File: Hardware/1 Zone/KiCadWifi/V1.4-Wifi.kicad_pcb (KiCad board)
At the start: 2 copper layers, 100 x 80 mm, 133 parts, among them CN11 Pinheader 1x12 P2.54 Horizont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, CN16 Pinheader 1x02 P2.54 Horizont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, J1 Screw_Terminal_01x02, Q1 IPD90N04S403ATMA1, Q10 PJA3404A, Q11 PJA3404A, Q12 BC816-16VL, Q8 UMH3NTN, SW1 K2-1102DP-G3SW-04, SW2 K2-1102DP-G3SW-04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

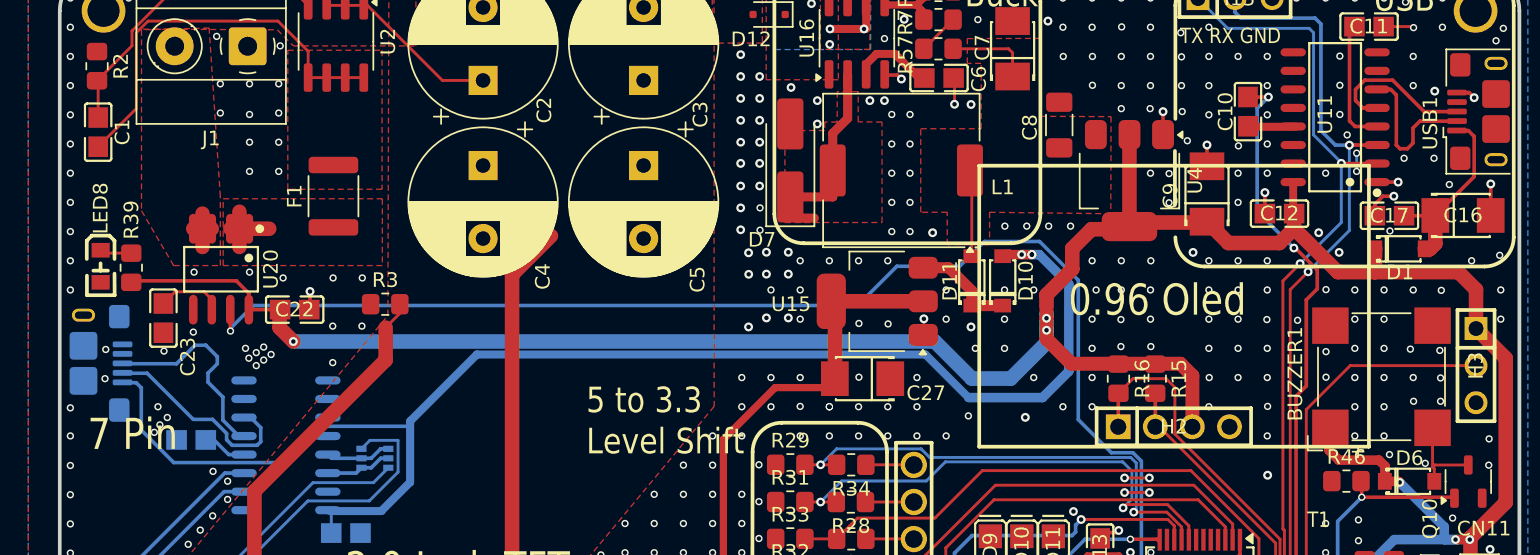
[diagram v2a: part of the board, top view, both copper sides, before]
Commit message: Rerouted D+,D-,E_D+,E_D- differential pairs to reduce gap between them. Renamed D+_E, D-_E for KiCad reasons.
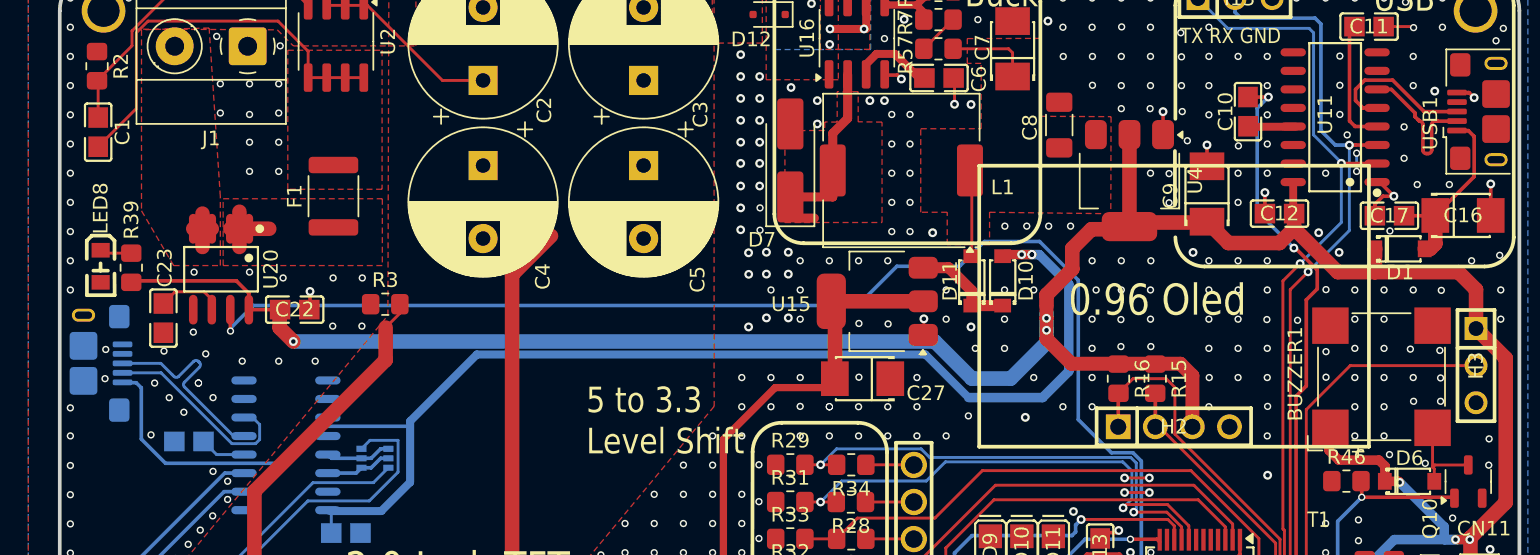
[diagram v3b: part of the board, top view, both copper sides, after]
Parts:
- moved C31 0.18 mm to (108.8, 102.5)
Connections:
- net D+_E renamed E_D+
- net D-_E renamed E_D-
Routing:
- net Net-(U22-V3): track 2.46 -> 3.14 mm
- net GND: track 59.8 -> 59.9 mm, vias 697 -> 696
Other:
- board text removed: "7 Pin"

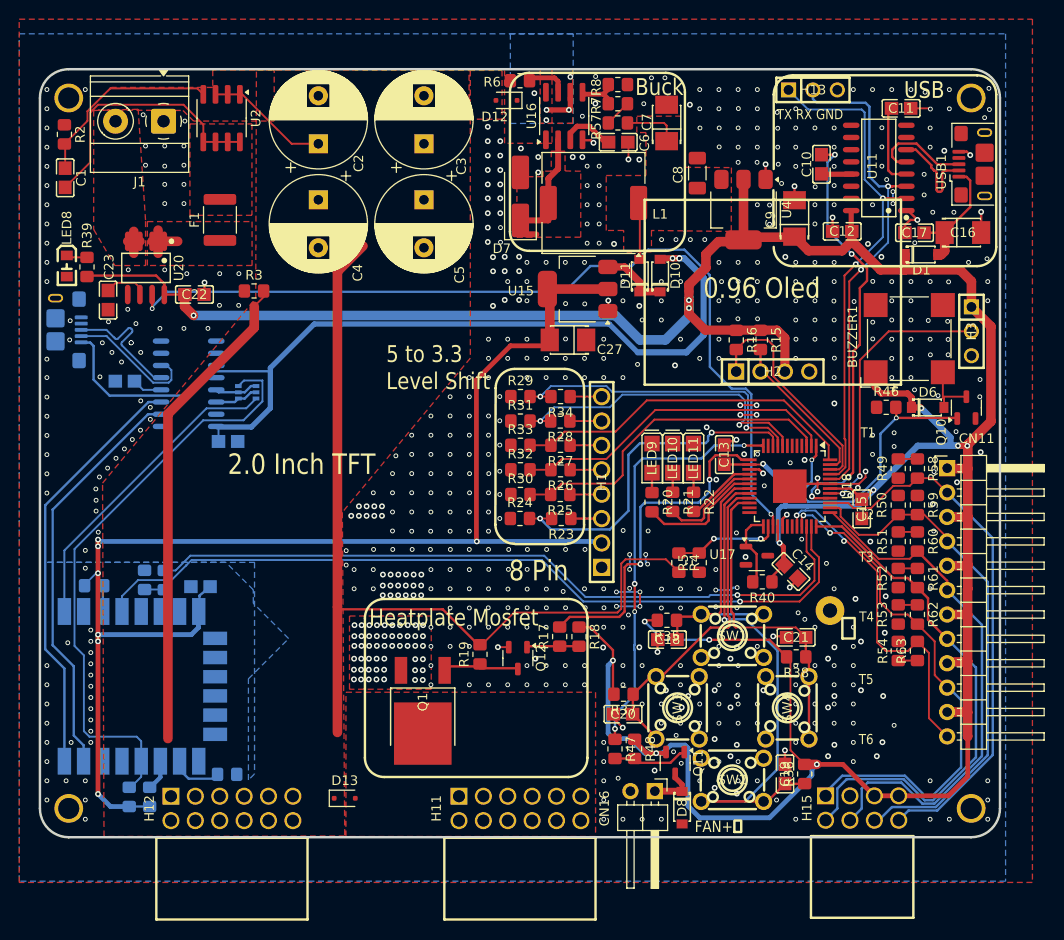
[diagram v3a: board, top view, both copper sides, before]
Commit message: Refactor. Visual improvements to PCB layout.
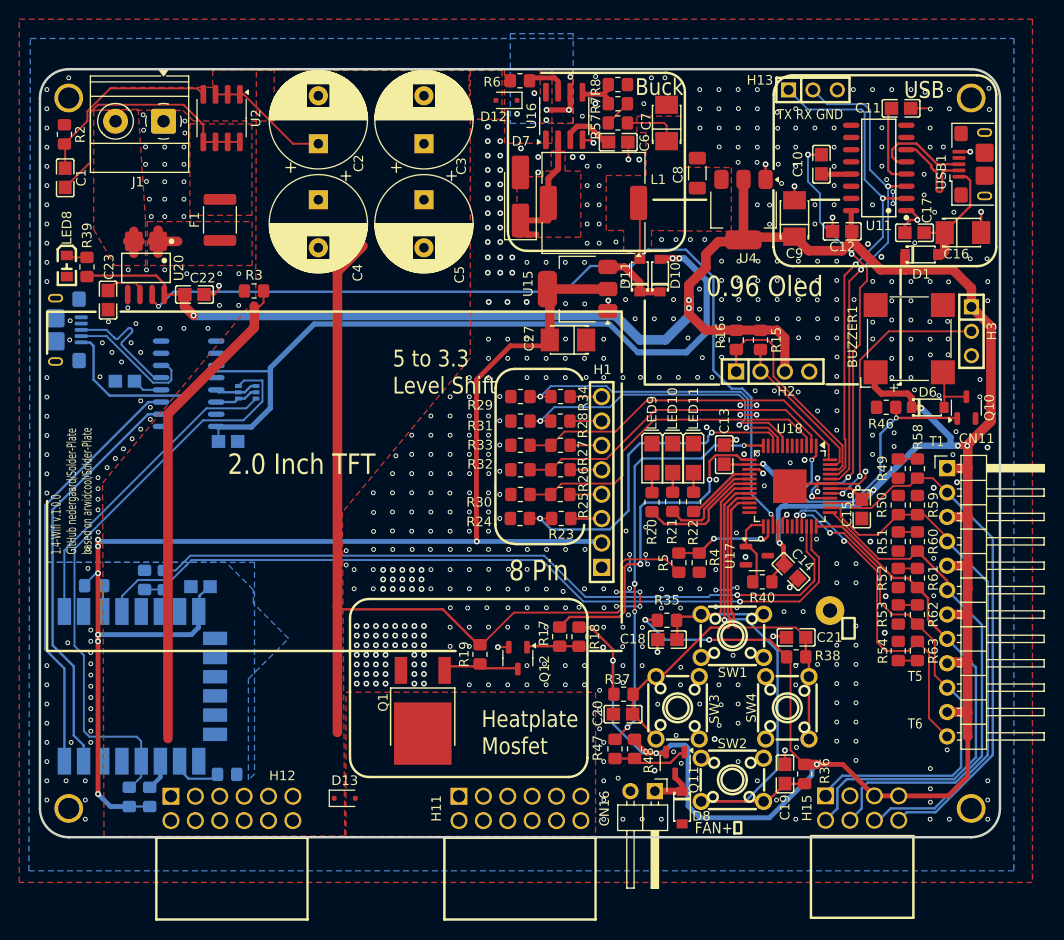
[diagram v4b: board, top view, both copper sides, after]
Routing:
- net THERMISTOR5: track 53.5 -> 51.7 mm
- net THERMISTOR3: track 54.9 -> 53.0 mm
- net THERMISTOR4: track 54.8 -> 53.0 mm
- net +5V: track 361.4 -> 359.8 mm
- net RXD: track 52.3 -> 51.1 mm
- net CURRENT_READ: track 92.9 -> 92.0 mm
- net RST: track 44.7 -> 45.2 mm
- net VUSB_ESP: track 97.6 -> 97.9 mm, vias 3 -> 2
- net GND: vias 696 -> 655
- net VIN: vias 5 -> 6
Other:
- board text added: "1.4-Wifi v.1.0.0 GitHub nedergaard/Solder-Plate based on arwidcool/Solder-Plate"
- board text removed: "T2"
- board text removed: "T3"
- board text removed: "T4"

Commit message: Refactor. Visual improvements to PCB layout
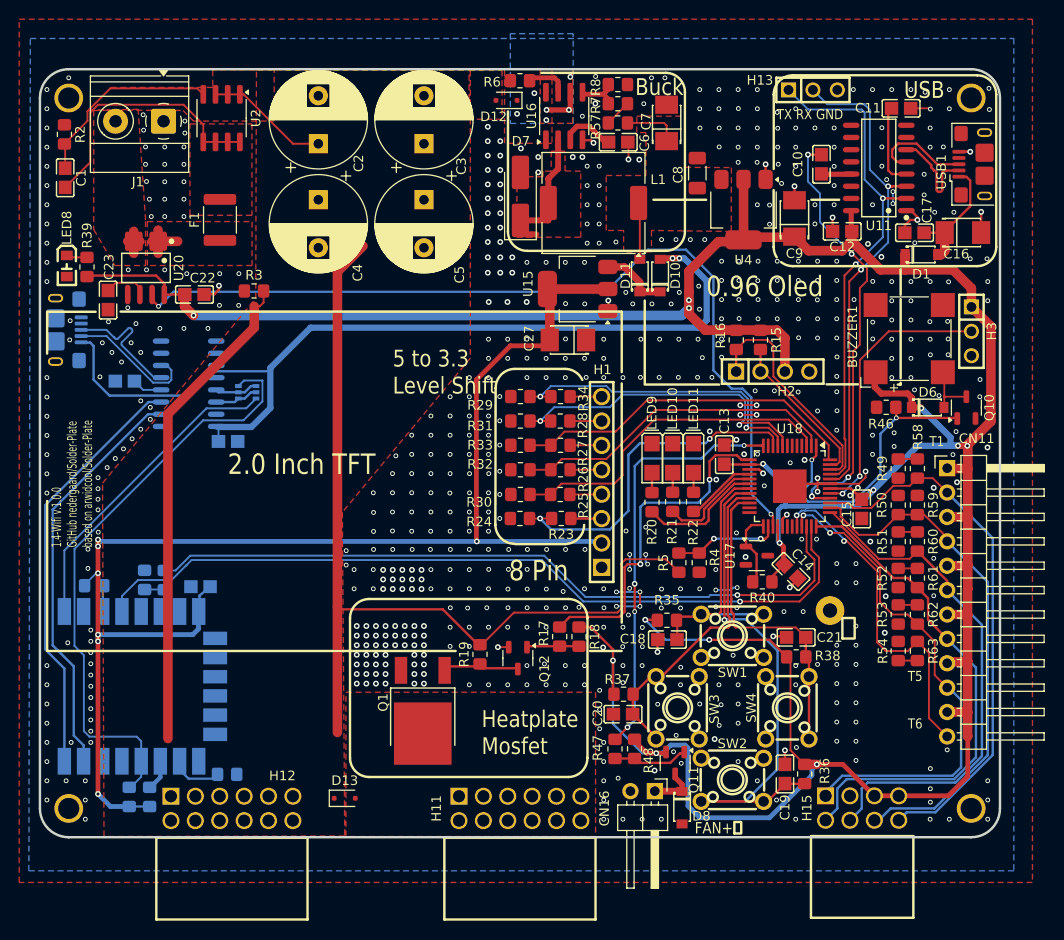
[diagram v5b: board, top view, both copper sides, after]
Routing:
- net VUSB_ESP: track 97.9 -> 95.0 mm
- net +5V: track 359.8 -> 357.2 mm
- net GND: vias 655 -> 657
